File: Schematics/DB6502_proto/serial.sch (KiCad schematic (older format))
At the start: 15 parts, among them J10 LCD Port, J11 VIA Ports, U18 SC26C92, U19 65C22S, U8 74AC04, Y2 3,6864MHz

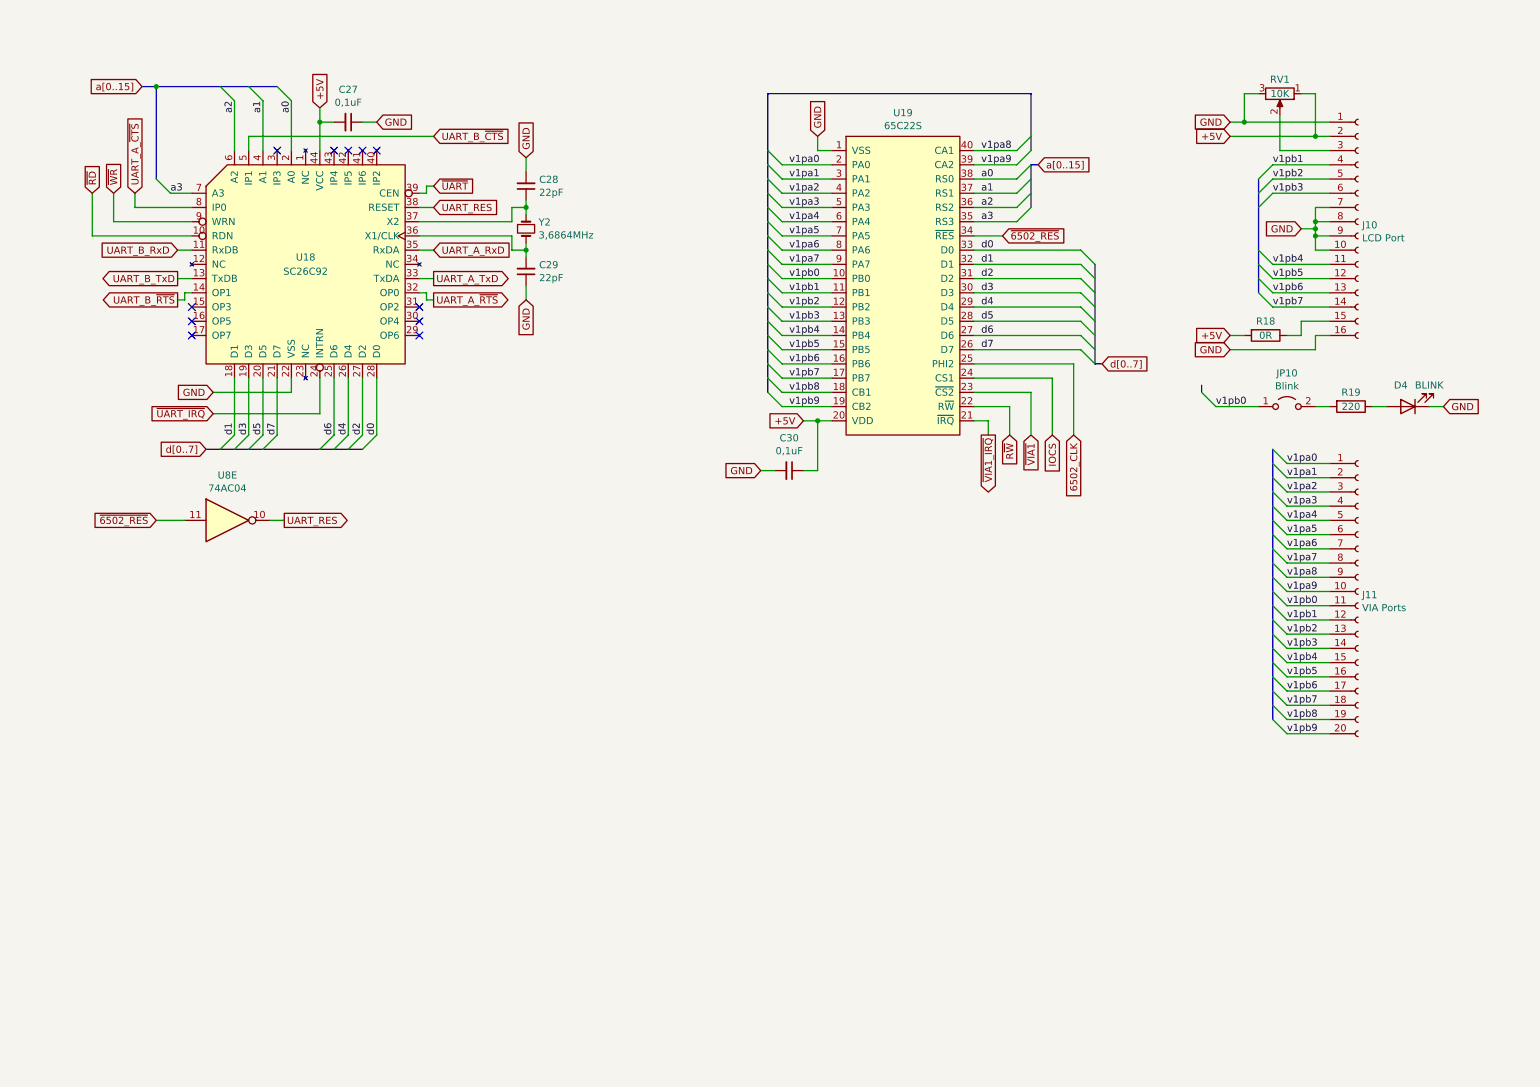
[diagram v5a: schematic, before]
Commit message: Redesigned jumpers, introduced resistor network
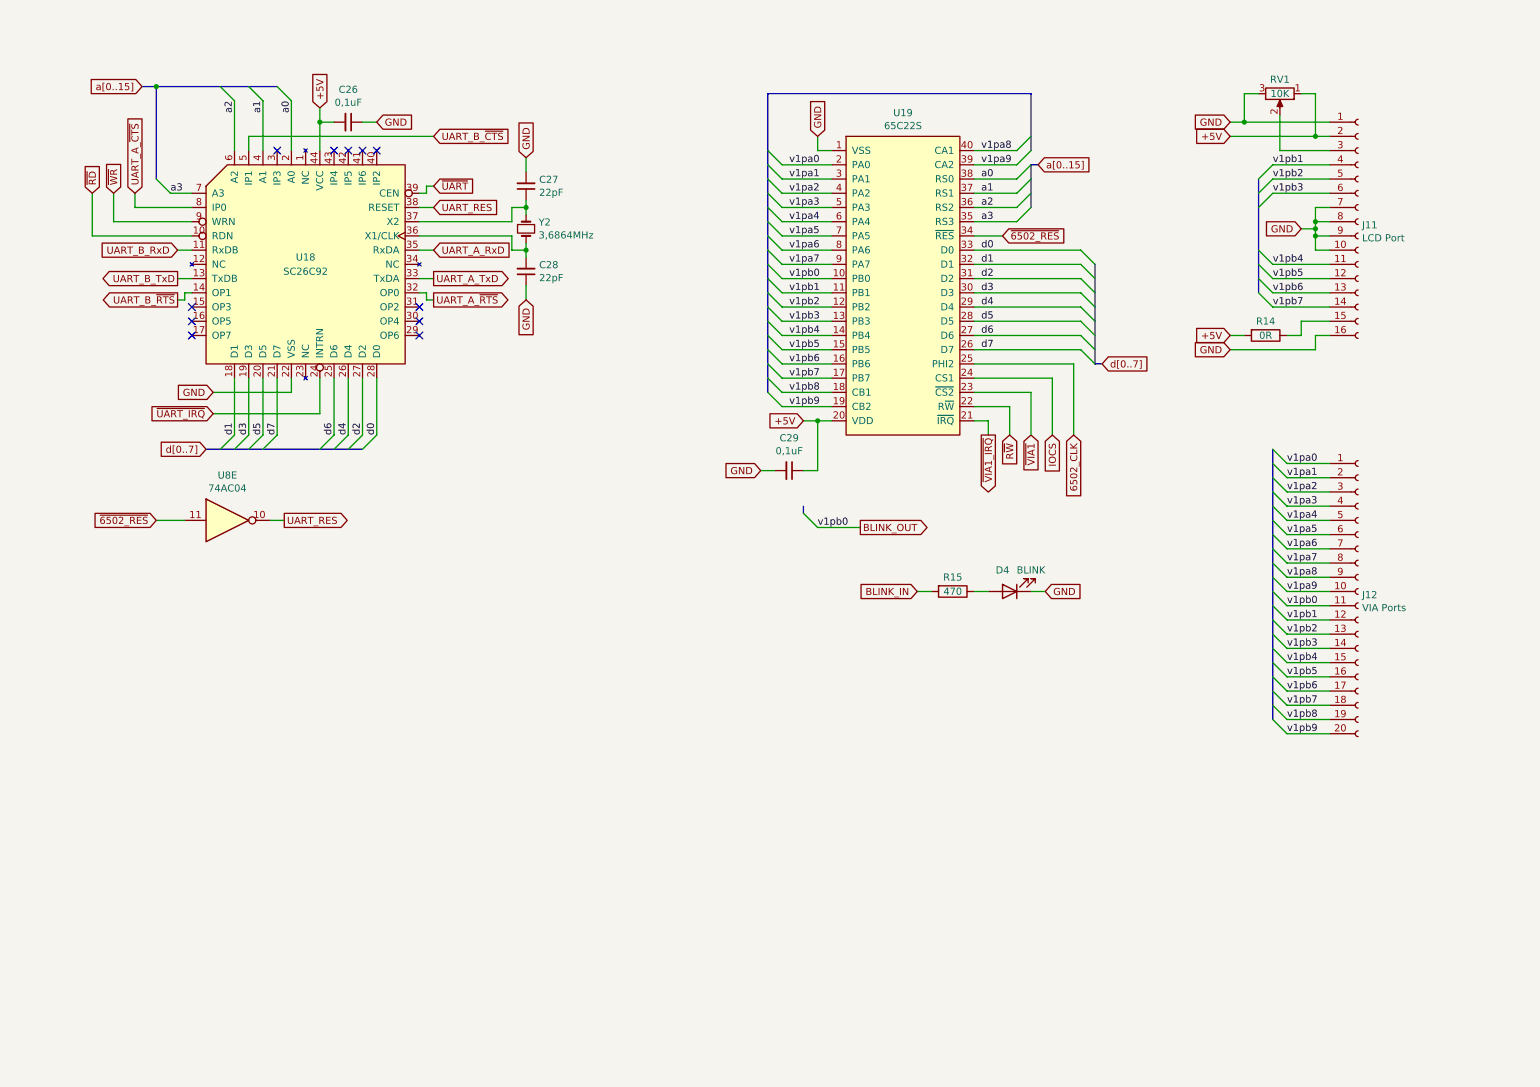
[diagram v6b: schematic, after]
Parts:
- removed JP10: Blink, Connector_PinHeader_2.54mm:PinHeader_2x01_P2.54mm_Vertical, symbol Jumper:Jumper_2_Open
- R15: renamed from R19; value 220 -> 470
- renumbered C27 to C26, C28 to C27, C29 to C28, C30 to C29, J10 to J11, J11 to J12, R18 to R14
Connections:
- net BLINK_IN: now reaches R15.2
- net v1pb0 renamed BLINK_OUT
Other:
- moved on the sheet: D4, R15
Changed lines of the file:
@@
 	2500 950  2500 1050
 $Comp
-L Device:C_Small C27
+L Device:C_Small C26
 U 1 1 5F932BB1
 P 2700 1050
-F 0 "C27" V 2471 1050 50  0000 C CNN
+F 0 "C26" V 2471 1050 50  0000 C CNN
 F 1 "0,1uF" V 2562 1050 50  0000 C CNN
 F 2 "Capacitor_SMD:C_1206_3216Metric_Pad1.42x1.75mm_HandSolder" H 2700 1050 50  0001 C CNN
@@
 $EndComp
 $Comp
-L Device:C_Small C28
+L Device:C_Small C27
 U 1 1 5F93E98E
 P 3950 1500
-F 0 "C28" H 3858 1454 50  0000 R CNN
+F 0 "C27" H 3858 1454 50  0000 R CNN
 F 1 "22pF" H 3858 1545 50  0000 R CNN
 F 2 "Capacitor_THT:C_Disc_D5.0mm_W2.5mm_P2.50mm" H 3950 1500 50  0001 C CNN
@@
 $EndComp
 $Comp
-L Device:C_Small C29
+L Device:C_Small C28
 U 1 1 5F93F1BF
 P 3950 2100
-F 0 "C29" H 3858 2054 50  0000 R CNN
+F 0 "C28" H 3858 2054 50  0000 R CNN
 F 1 "22pF" H 3858 2145 50  0000 R CNN
 F 2 "Capacitor_THT:C_Disc_D5.0mm_W2.5mm_P2.50mm" H 3950 2100 50  0001 C CNN
@@
 	5900 3150 6000 3150
 $Comp
-L Device:C_Small C30
+L Device:C_Small C29
 U 1 1 60B853CC
 P 5800 3500
-F 0 "C30" V 5571 3500 50  0000 C CNN
+F 0 "C29" V 5571 3500 50  0000 C CNN
 F 1 "0,1uF" V 5662 3500 50  0000 C CNN
 F 2 "Capacitor_SMD:C_1206_3216Metric_Pad1.42x1.75mm_HandSolder" H 5800 3500 50  0001 C CNN
@@
 	5650 850  7500 850
 $Comp
-L Connector:Conn_01x16_Female J10
+L Connector:Conn_01x16_Female J11
 U 1 1 60BD0212
 P 9800 1750
-F 0 "J10" H 9828 1726 50  0000 L CNN
+F 0 "J11" H 9828 1726 50  0000 L CNN
 F 1 "LCD Port" H 9828 1635 50  0000 L CNN
 F 2 "Connector_PinSocket_2.54mm:PinSocket_1x16_P2.54mm_Vertical" H 9800 1750 50  0001 C CNN
@@
 	9500 2550 9600 2550
 $Comp
-L Device:R R18
+L Device:R R14
 U 1 1 60BF69A9
 P 9150 2550
-F 0 "R18" V 9050 2550 50  0000 C CNN
+F 0 "R14" V 9050 2550 50  0000 C CNN
 F 1 "0R" V 9150 2550 50  0000 C CNN
 F 2 "Resistor_THT:R_Axial_DIN0207_L6.3mm_D2.5mm_P10.16mm_Horizontal" V 9080 2550 50  0001 C CNN
@@
 Wire Wire Line
 	9200 1350 9600 1350
-Text Label 8800 3050 0    50   ~ 0
+Text Label 6000 3900 0    50   ~ 0
 v1pb0
 $Comp
-L Device:R R19
+L Device:R R15
 U 1 1 60C63461
-P 9750 3050
-F 0 "R19" V 9650 3050 50  0000 C CNN
-F 1 "220" V 9750 3050 50  0000 C CNN
-F 2 "Resistor_THT:R_Axial_DIN0207_L6.3mm_D2.5mm_P10.16mm_Horizontal" V 9680 3050 50  0001 C CNN
-F 3 "~" H 9750 3050 50  0001 C CNN
-	1    9750 3050
+P 6950 4350
+F 0 "R15" V 6850 4350 50  0000 C CNN
+F 1 "470" V 6950 4350 50  0000 C CNN
+F 2 "Resistor_THT:R_Axial_DIN0207_L6.3mm_D2.5mm_P10.16mm_Horizontal" V 6880 4350 50  0001 C CNN
+F 3 "~" H 6950 4350 50  0001 C CNN
+	1    6950 4350
 	0    1    1    0
 $EndComp
 Wire Wire Line
-	9900 3050 10000 3050
+	7100 4350 7200 4350
 $Comp
 L Device:LED D4
 U 1 1 60C6A184
-P 10150 3050
-F 0 "D4" H 10200 2900 50  0000 C CNN
-F 1 "BLINK" H 10000 2900 50  0000 C CNN
-F 2 "LED_THT:LED_D3.0mm" H 10150 3050 50  0001 C CNN
-F 3 "~" H 10150 3050 50  0001 C CNN
-	1    10150 3050
+P 7350 4350
+F 0 "D4" H 7400 4200 50  0000 C CNN
+F 1 "BLINK" H 7200 4200 50  0000 C CNN
+F 2 "LED_THT:LED_D3.0mm" H 7350 4350 50  0001 C CNN
+F 3 "~" H 7350 4350 50  0001 C CNN
+	1    7350 4350
 	-1   0    0    1
 $EndComp
-Text GLabel 10400 3050 2    50   Input ~ 0
-GND
-Wire Wire Line
-	10300 3050 10400 3050
-Entry Wire Line
-	8700 2950 8800 3050
-Wire Bus Line
-	8700 2950 8700 2900
-$Comp
-L Connector:Conn_01x20_Female J11
+Text GLabel 7600 4350 2    50   Input ~ 0
+GND
+Wire Wire Line
+	7500 4350 7600 4350
+Entry Wire Line
+	5900 3800 6000 3900
+Wire Bus Line
+	5900 3800 5900 3750
+$Comp
+L Connector:Conn_01x20_Female J12
 U 1 1 60C83532
 P 9800 4350
-F 0 "J11" H 9828 4326 50  0000 L CNN
+F 0 "J12" H 9828 4326 50  0000 L CNN
 F 1 "VIA Ports" H 9828 4235 50  0000 L CNN
 F 2 "Connector_PinSocket_2.54mm:PinSocket_1x20_P2.54mm_Vertical" H 9800 4350 50  0001 C CNN
@@
 	1    0    0    -1
 $EndComp
-$Comp
-L Jumper:Jumper_2_Open JP10
-U 1 1 60C9E672
-P 9300 3050
-F 0 "JP10" H 9300 3285 50  0000 C CNN
-F 1 "Blink" H 9300 3194 50  0000 C CNN
-F 2 "Connector_PinHeader_2.54mm:PinHeader_2x01_P2.54mm_Vertical" H 9300 3050 50  0001 C CNN
-F 3 "~" H 9300 3050 50  0001 C CNN
-	1    9300 3050
-	1    0    0    -1
-$EndComp
-Wire Wire Line
-	8800 3050 9100 3050
-Wire Wire Line
-	9500 3050 9600 3050
+Wire Wire Line
+	6000 3900 6300 3900
+Wire Wire Line
+	6700 4350 6800 4350
 Text Label 9300 3450 0    50   ~ 0
 v1pa0
@@
 Wire Bus Line
 	5650 850  5650 2950
+Text GLabel 6300 3900 2    50   Output ~ 0
+BLINK_OUT
+Text GLabel 6700 4350 0    50   Input ~ 0
+BLINK_IN
 $EndSCHEMATC

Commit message: Working on a PCB
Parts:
- RV1: footprint Potentiometer_THT:Potentiometer_Piher_PT-10-V10_Vertical -> Potentiometer_THT:Potentiometer_Bourns_3386F_Vertical
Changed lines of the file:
@@
 F 0 "RV1" V 9150 850 50  0000 C CNN
 F 1 "10K" V 9250 850 50  0000 C CNN
-F 2 "Potentiometer_THT:Potentiometer_Piher_PT-10-V10_Vertical" H 9250 850 50  0001 C CNN
+F 2 "Potentiometer_THT:Potentiometer_Bourns_3386F_Vertical" H 9250 850 50  0001 C CNN
 F 3 "~" H 9250 850 50  0001 C CNN
 	1    9250 850
@@
 Entry Wire Line
 	9200 5250 9300 5350
-Wire Bus Line
-	7500 850  7500 1250
-Wire Bus Line
-	1350 800  2200 800
-Wire Bus Line
-	7500 1350 7500 1650
-Wire Bus Line
-	7950 2050 7950 2750
-Wire Bus Line
-	9100 1450 9100 2250
-Wire Bus Line
-	1700 3350 2800 3350
-Wire Bus Line
-	9200 3350 9200 5250
-Wire Bus Line
-	5650 850  5650 2950
 Text GLabel 6300 3900 2    50   Output ~ 0
 BLINK_OUT
 Text GLabel 6700 4350 0    50   Input ~ 0
 BLINK_IN
+Wire Bus Line
+	7500 850  7500 1250
+Wire Bus Line
+	1350 800  2200 800
+Wire Bus Line
+	7500 1350 7500 1650
+Wire Bus Line
+	7950 2050 7950 2750
+Wire Bus Line
+	9100 1450 9100 2250
+Wire Bus Line
+	1700 3350 2800 3350
+Wire Bus Line
+	9200 3350 9200 5250
+Wire Bus Line
+	5650 850  5650 2950
 $EndSCHEMATC

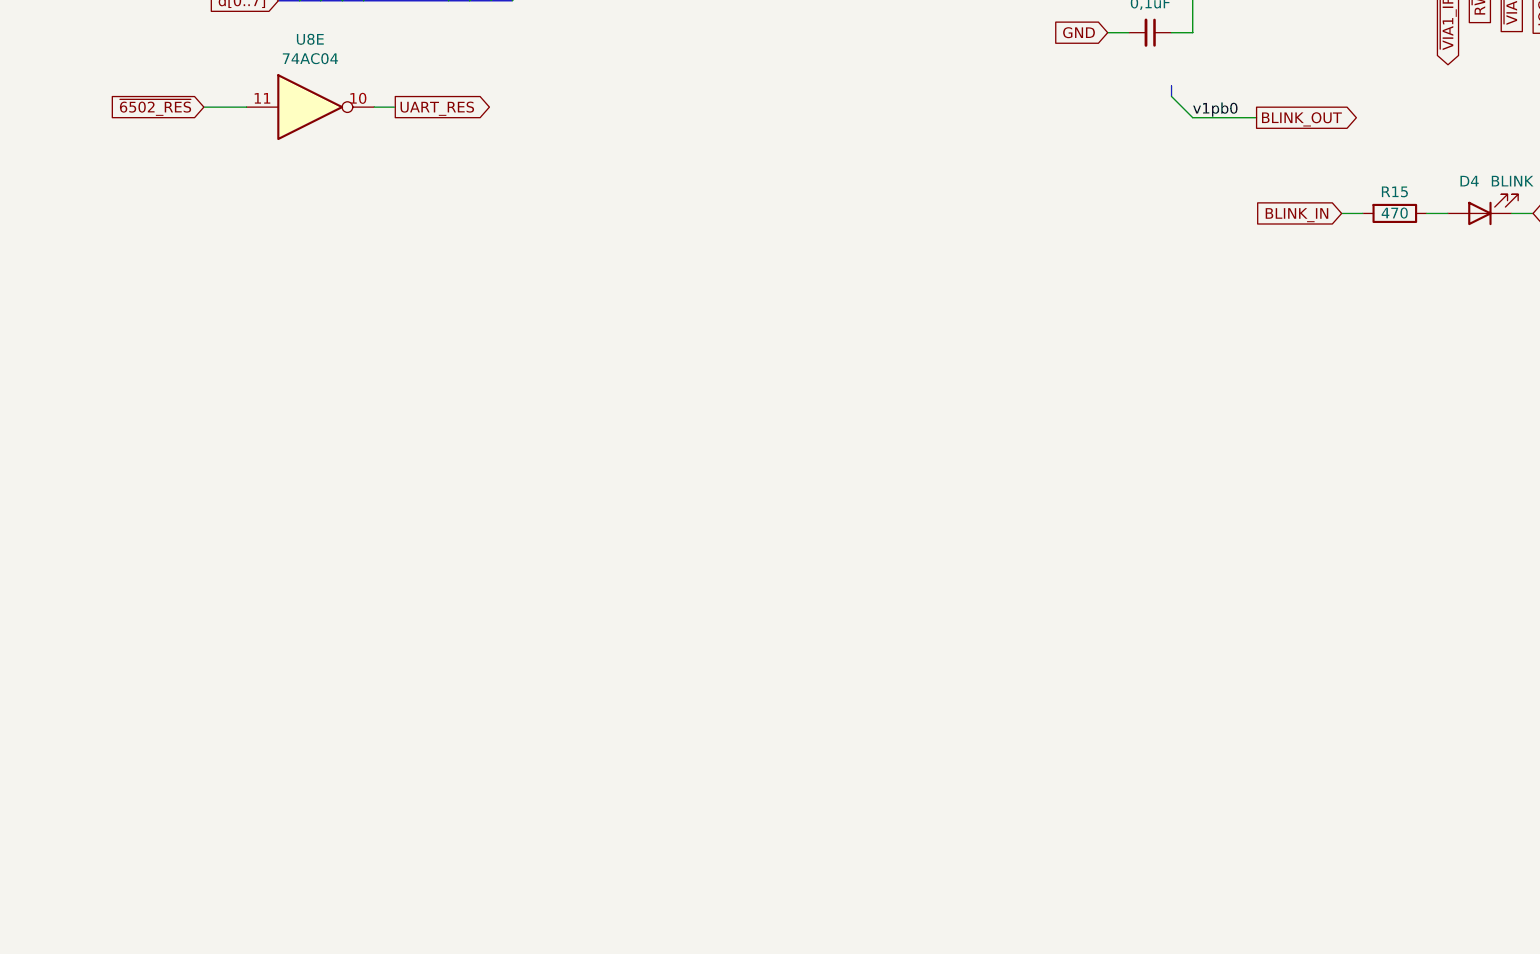
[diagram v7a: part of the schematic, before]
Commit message: Added latch feature for EXRAM
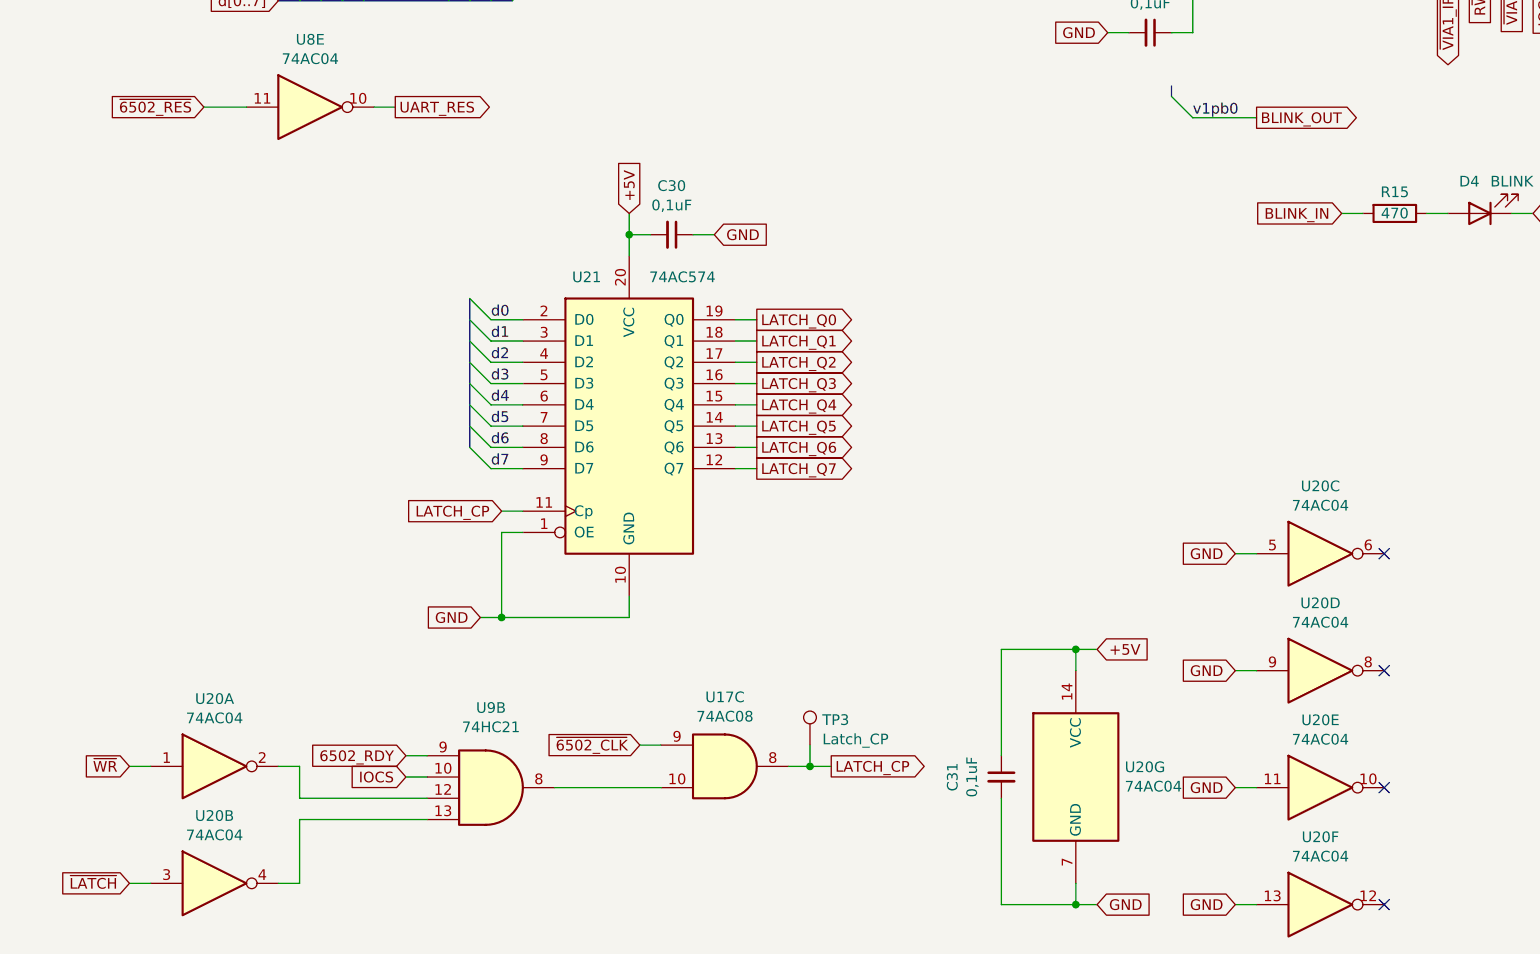
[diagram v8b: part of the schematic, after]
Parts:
- added C30, C31: 0,1uF, Capacitor_SMD:C_1206_3216Metric_Pad1.42x1.75mm_HandSolder, symbol Device:C_Small
- added TP3: Latch_CP, TestPoint:TestPoint_Keystone_5005-5009_Compact, symbol Connector:TestPoint
- added U17: 74AC08, Package_SO:SOIC-14_3.9x8.7mm_P1.27mm, symbol 74xx:74LS08
- added U20: 74AC04, Package_SO:SOIC-14_3.9x8.7mm_P1.27mm, symbol 74xx:74HC04
- added U21: 74AC574, Package_SO:SOIC-20W_7.5x12.8mm_P1.27mm, symbol 74xx:74HCT574
- added U9: 74HC21, Package_SO:SOIC-14_3.9x8.7mm_P1.27mm, symbol 74xx:74LS21
- R15: footprint Resistor_THT:R_Axial_DIN0207_L6.3mm_D2.5mm_P10.16mm_Horizontal -> Resistor_SMD:R_1206_3216Metric_Pad1.42x1.75mm_HandSolder
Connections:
- net +5V: now also C30.2, C31.1, U20.14 (VCC), U21.20 (VCC)
- net GND: now also C30.1, C31.2, U20.11, U20.13, U20.5, U20.7 (GND), U20.9, U21.1 (OE), U21.10 (GND)
- net IOCS: now also U9.10
- net d0: now also U21.2 (D0)
- net d1: now also U21.3 (D1)
- net d2: now also U21.4 (D2)
- net d3: now also U21.5 (D3)
- net d4: now also U21.6 (D4)
- net d5: now also U21.7 (D5)
- net d6: now also U21.8 (D6)
- net d7: now also U21.9 (D7)
- net ~WR: now also U20.1
- new net: U20.2, U9.12
- new net: U20.4, U9.13
- new net: U17.10, U9.8
- new net 6502_RDY: U9.9
- new net LATCH_CP: TP3.1, U17.8, U21.11 (Cp)
- new net LATCH_Q0: U21.19 (Q0)
- new net LATCH_Q1: U21.18 (Q1)
- new net LATCH_Q2: U21.17 (Q2)
- new net LATCH_Q3: U21.16 (Q3)
- new net LATCH_Q4: U21.15 (Q4)
- new net LATCH_Q5: U21.14 (Q5)
- new net LATCH_Q6: U21.13 (Q6)
- new net LATCH_Q7: U21.12 (Q7)
- new net ~6502_CLK: U17.9
- new net ~LATCH: U20.3
- no-connect marks 11 -> 15
